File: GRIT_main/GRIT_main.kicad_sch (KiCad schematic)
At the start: 1 part, among them J1 Raspberry_Pi_4

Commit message: Updated Schematic
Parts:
- added BT1: Battery, symbol Device:Battery
- added Buck_Converter: ~, symbol Custom_Symbols:Buck_Converter_12V_to_5V
- added F1: Fuse, symbol Device:Fuse
- added M1, M2: Motor_DC, symbol Motor:Motor_DC
- added Motor_Driver_1, Motor_Driver_2, Motor_Driver_3, Motor_Driver_4: ~, symbol Custom_Symbols:12V_Motor_Controller
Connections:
- net at J1.32 (GPIO12/PWM0): now also Motor_Driver_1.3 (RPWM), Motor_Driver_1.4 (LPWM)
- net at J1.33 (GPIO13/PWM1): now also Motor_Driver_2.3 (RPWM), Motor_Driver_2.4 (LPWM)
- new net: Buck_Converter. (4), F1.1, Motor_Driver_1.2 (B+), Motor_Driver_2.2 (B+)
- new net: Buck_Converter. (4), Motor_Driver_1.1 (Vcc), Motor_Driver_2.1 (Vcc)
- new net: BT1.2 (-), Buck_Converter. (4), Motor_Driver_1.7 (B-), Motor_Driver_2.7 (B-)
- new net: Buck_Converter. (4), Motor_Driver_1.8 (GND), Motor_Driver_2.8 (GND)
- new net: M2.1 (+), Motor_Driver_2.12 (M+)
- new net: M2.2 (-), Motor_Driver_2.11 (M-)
- new net: BT1.1 (+), F1.2
- new net: M1.1 (+), Motor_Driver_1.12 (M+)
- new net: M1.2 (-), Motor_Driver_1.11 (M-)
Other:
- moved on the sheet: J1

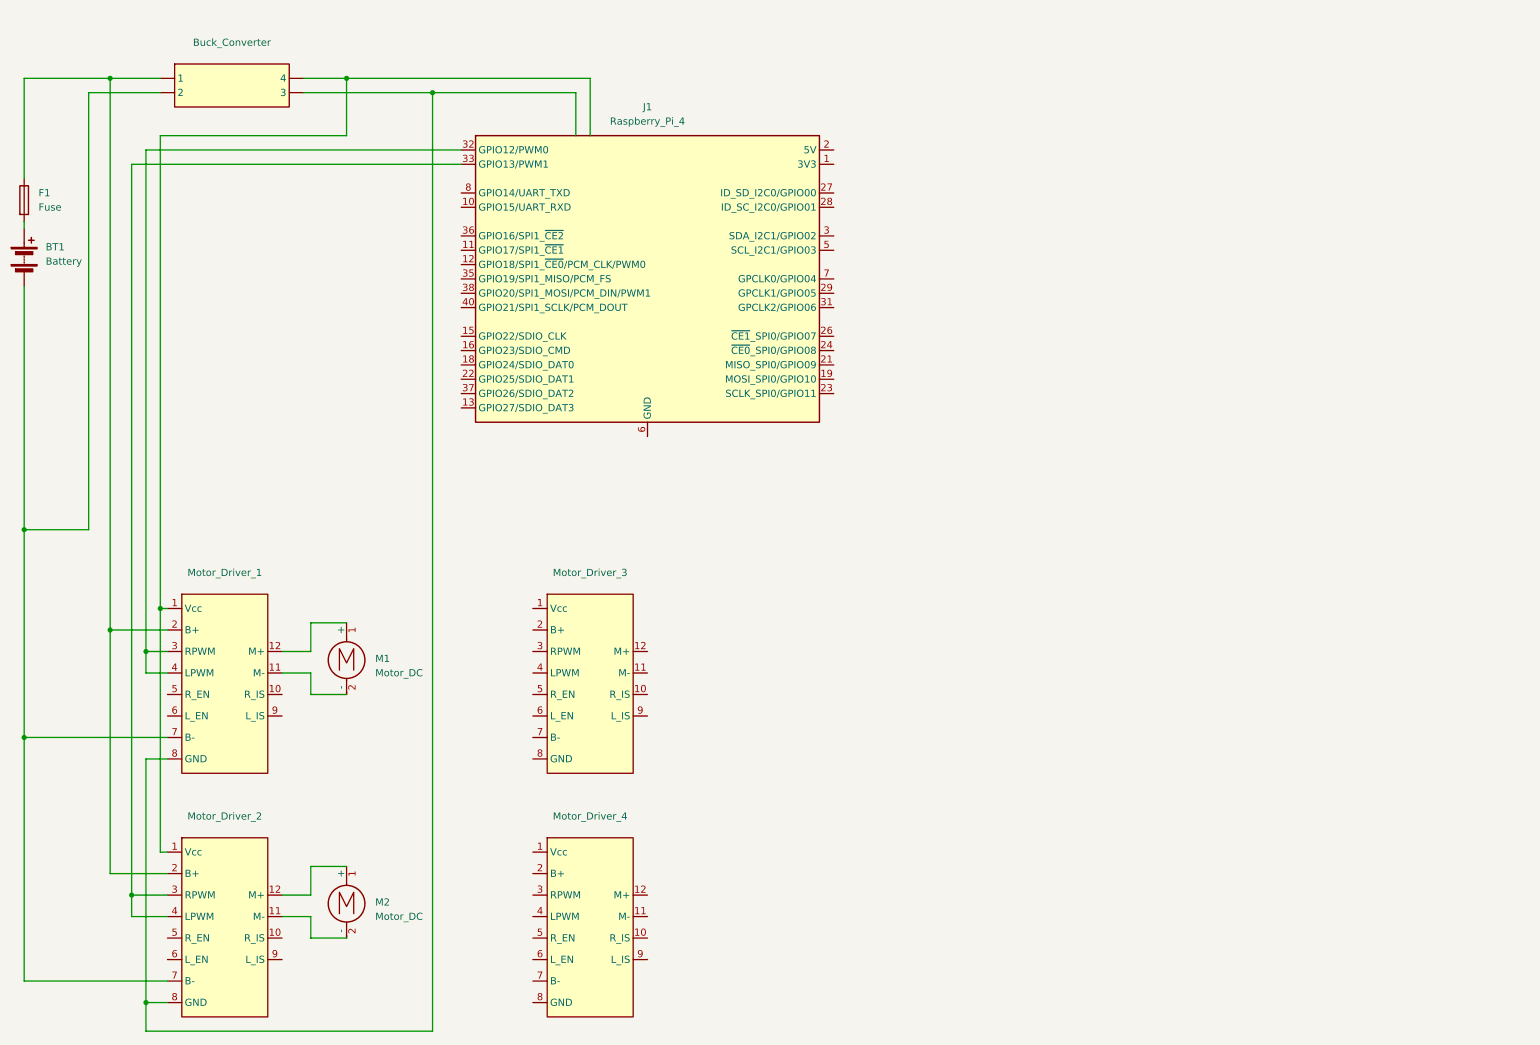
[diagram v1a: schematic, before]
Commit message: Updated Schematic
Added GPS, IMU, and Ultrasonic sensors to schematic. Also wired the other two motor drivers to the motors.
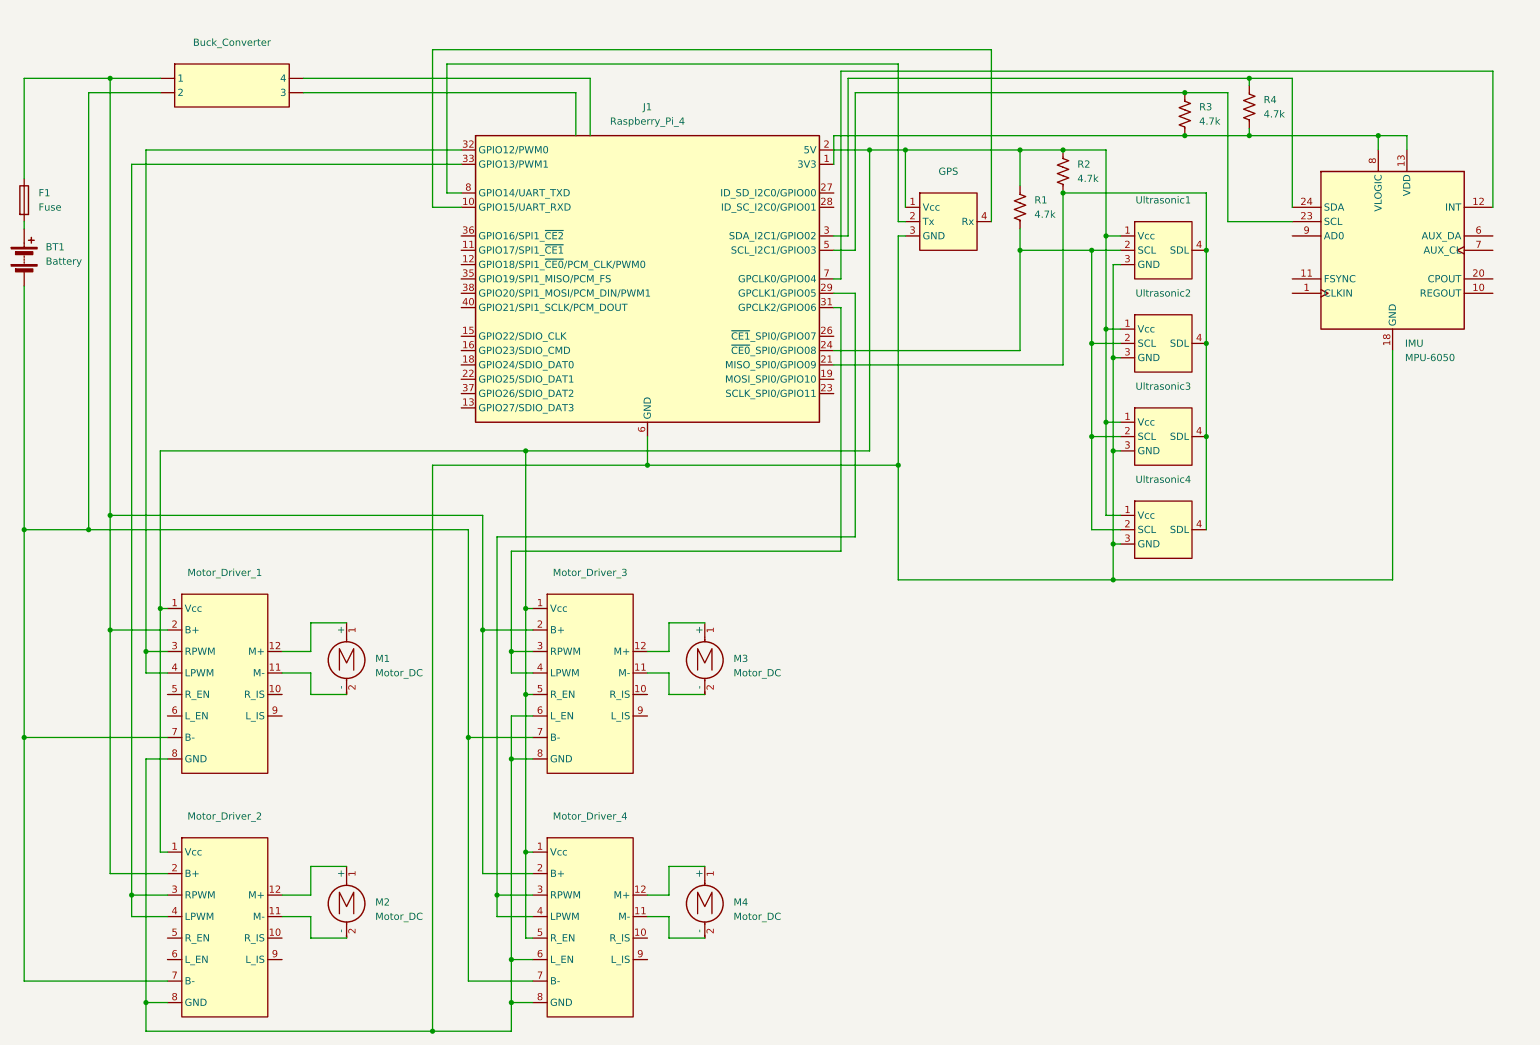
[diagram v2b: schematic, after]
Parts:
- added GPS: ~, symbol Custom_Symbols:NEO_6M_GPS
- added IMU: MPU-6050, Sensor_Motion:InvenSense_QFN-24_4x4mm_P0.5mm, symbol Sensor_Motion:MPU-6050
- added M3, M4: Motor_DC, symbol Motor:Motor_DC
- added R1, R2, R3, R4: 4.7k, symbol Device:R_US
- added Ultrasonic1, Ultrasonic2, Ultrasonic3, Ultrasonic4: ~, symbol Custom_Symbols:I2C_Ultrasonic_Sensor
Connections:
- net at Motor_Driver_3.1 (Vcc): now also J1.2 (5V), J1.4 (5V), Motor_Driver_1.1 (Vcc), Motor_Driver_2.1 (Vcc), Motor_Driver_3.5 (R_EN), Motor_Driver_4.1 (Vcc), Motor_Driver_4.5 (R_EN), GPS.1 (Vcc), R1.1, R2.1, Ultrasonic1.1 (Vcc), Ultrasonic2.1 (Vcc), Ultrasonic3.1 (Vcc), Ultrasonic4.1 (Vcc)
- net at Motor_Driver_3.11 (M-): now also M3.2 (-)
- net at Motor_Driver_3.12 (M+): now also M3.1 (+)
- net at Motor_Driver_3.2 (B+): now also Buck_Converter. (4), F1.1, Motor_Driver_1.2 (B+), Motor_Driver_2.2 (B+), Motor_Driver_4.2 (B+)
- net at Motor_Driver_3.3 (RPWM): now also J1.31 (GPCLK2/GPIO06), Motor_Driver_3.4 (LPWM)
- net at Motor_Driver_3.6 (L_EN): now also J1.14 (GND), J1.20 (GND), J1.25 (GND), J1.30 (GND), J1.34 (GND), J1.39 (GND), J1.6 (GND), J1.9 (GND), Motor_Driver_1.8 (GND), Motor_Driver_2.8 (GND), Motor_Driver_3.8 (GND), Motor_Driver_4.6 (L_EN), Motor_Driver_4.8 (GND), GPS.3 (GND), IMU.18 (GND), Ultrasonic1.3 (GND), Ultrasonic2.3 (GND), Ultrasonic3.3 (GND), Ultrasonic4.3 (GND)
- net at Motor_Driver_3.7 (B-): now also BT1.2 (-), Buck_Converter. (4), Motor_Driver_1.7 (B-), Motor_Driver_2.7 (B-), Motor_Driver_4.7 (B-)
- net at Motor_Driver_4.11 (M-): now also M4.2 (-)
- net at Motor_Driver_4.12 (M+): now also M4.1 (+)
- net at Motor_Driver_4.3 (RPWM): now also J1.29 (GPCLK1/GPIO05), Motor_Driver_4.4 (LPWM)
- net at J1.1 (3V3), J1.17 (3V3): now also IMU.13 (VDD), IMU.8 (VLOGIC), R3.2, R4.2
- net at J1.10 (GPIO15/UART_RXD): now also GPS.4 (Rx)
- net at J1.21 (MISO_SPI0/GPIO09): now also R2.2, Ultrasonic1.4 (SDL), Ultrasonic2.4 (SDL), Ultrasonic3.4 (SDL), Ultrasonic4.4 (SDL)
- net at J1.24 (~{CE0}_SPI0/GPIO08): now also R1.2, Ultrasonic1.2 (SCL), Ultrasonic2.2 (SCL), Ultrasonic3.2 (SCL), Ultrasonic4.2 (SCL)
- net at J1.3 (SDA_I2C1/GPIO02): now also IMU.24 (SDA), R4.1
- net at J1.5 (SCL_I2C1/GPIO03): now also IMU.23 (SCL), R3.1
- net at J1.7 (GPCLK0/GPIO04): now also IMU.12 (INT)
- net at J1.8 (GPIO14/UART_TXD): now also GPS.2 (Tx)
- now unconnected: Buck_Converter. (4), Buck_Converter. (4), Buck_Converter. (4), Buck_Converter. (4)

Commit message: Updated Schematic
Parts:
- added D1, D2: LED, symbol Device:LED
- added LCD: ~, symbol Custom_Symbols:I2C_LCD_Screen
- added LimitSwitch: ~, symbol Switch:SW_SPDT_XKB_DMx-xxxx-1
- added Q1: IRLZ34N, Package_TO_SOT_THT:TO-220-3_Vertical, symbol Transistor_FET:IRLZ34N
- added Ultrasonic5, Ultrasonic6, Ultrasonic7: ~, symbol Custom_Symbols:I2C_Ultrasonic_Sensor
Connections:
- net at GPS.3 (GND), IMU.18 (GND), J1.14 (GND)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: now also LCD.3 (GND), LimitSwitch.1 (A), Ultrasonic5.3 (GND), Ultrasonic6.3 (GND), Ultrasonic7.3 (GND)
- net at GPS.1 (Vcc), J1.2 (5V), J1.4 (5V)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: now also LCD.1 (Vcc), Ultrasonic5.1 (Vcc), Ultrasonic6.1 (Vcc), Ultrasonic7.1 (Vcc)
- net at Buck_Converter. (4), F1.1, Motor_Driver_1.2 (B+)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: now also Q1.2 (D)
- net at BT1.2 (-), Buck_Converter. (4), Motor_Driver_1.7 (B-)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: now also D2.1 (K)
- net at J1.13 (GPIO27/SDIO_DAT3): now also LimitSwitch.3 (C)
- net at J1.19 (MOSI_SPI0/GPIO10): now also LCD.2 (SCL)
- net at J1.21 (MISO_SPI0/GPIO09), R2.2, Ultrasonic1.4 (SDL)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: now also Ultrasonic5.4 (SDL), Ultrasonic6.4 (SDL), Ultrasonic7.4 (SDL)
- net at J1.23 (SCLK_SPI0/GPIO11): now also LCD.4 (SDA)
- net at J1.24 (~{CE0}_SPI0/GPIO08), R1.2, Ultrasonic1.2 (SCL)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: now also Ultrasonic5.2 (SCL), Ultrasonic6.2 (SCL), Ultrasonic7.2 (SCL)
- net at J1.36 (GPIO16/SPI1_~{CE2}): now also Q1.1 (G)
- new net: D1.2 (A), Q1.3 (S)
- new net: D1.1 (K), D2.2 (A)
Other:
- moved on the sheet: BT1, F1

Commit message: Updated Design
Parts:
- removed Ultrasonic1, Ultrasonic2, Ultrasonic3, Ultrasonic4, Ultrasonic5, Ultrasonic6, Ultrasonic7: ~, symbol Custom_Symbols:I2C_Ultrasonic_Sensor
- added U1: Raspberry_Pi_Pico, Package_DFN_QFN:QFN-56-1EP_7x7mm_P0.4mm_EP3.2x3.2mm, symbol MCU_RaspberryPi:RP2040
- added US1, US2, US3, US4, US5, US6, US7: ~, symbol Custom_Symbols:I2C_Ultrasonic_Sensor
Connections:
- net at GPS.1 (Vcc), J1.2 (5V), J1.4 (5V)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: no longer R1.1, R2.1
- net at R1.2: now also J1.21 (MISO_SPI0/GPIO09), U1.28 (GPIO17); no longer J1.24 (~{CE0}_SPI0/GPIO08)
- net at GPS.3 (GND), IMU.18 (GND), J1.14 (GND)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: now also U1.57 (GND), US1.3 (GND), US2.3 (GND), US3.3 (GND), US4.3 (GND), US5.3 (GND), US6.3 (GND), US7.3 (GND)
- net at R2.2: now also J1.24 (~{CE0}_SPI0/GPIO08), U1.27 (GPIO16); no longer J1.21 (MISO_SPI0/GPIO09)
- net at IMU.13 (VDD), IMU.8 (VLOGIC), J1.1 (3V3)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: now also R1.1, R2.1
- net at IMU.23 (SCL), J1.5 (SCL_I2C1/GPIO03): now also R4.1; no longer R3.1
- net at IMU.24 (SDA), J1.3 (SDA_I2C1/GPIO02): now also R3.1; no longer R4.1
- new net: U1.4 (GPIO2), US1.1 (Trig)
- new net: U1.5 (GPIO3), US1.2 (Echo)
- new net: Buck_Converter. (4), U1.48 (USB_VDD), US1.4 (Vcc), US2.4 (Vcc), US3.4 (Vcc), US4.4 (Vcc), US5.4 (Vcc), US6.4 (Vcc), US7.4 (Vcc)
- new net: U1.15 (GPIO12), US6.1 (Trig)
- new net: U1.16 (GPIO13), US6.2 (Echo)
- new net: U1.6 (GPIO4), US2.1 (Trig)
- new net: U1.7 (GPIO5), US2.2 (Echo)
- new net: U1.17 (GPIO14), US7.1 (Trig)
- new net: U1.18 (GPIO15), US7.2 (Echo)
- new net: U1.11 (GPIO8), US4.1 (Trig)
- new net: U1.12 (GPIO9), US4.2 (Echo)
- new net: U1.8 (GPIO6), US3.1 (Trig)
- new net: U1.9 (GPIO7), US3.2 (Echo)
- new net: U1.1 (IOVDD), U1.10 (IOVDD), U1.22 (IOVDD), U1.33 (IOVDD), U1.42 (IOVDD), U1.49 (IOVDD)
- new net: U1.13 (GPIO10), US5.1 (Trig)
- new net: U1.14 (GPIO11), US5.2 (Echo)
- new net: U1.23 (DVDD), U1.50 (DVDD)
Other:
- moved on the sheet: IMU, LCD, LimitSwitch

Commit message: Updated and Added PDF
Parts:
- removed R3, R4: 4.7k, symbol Device:R_US
- M1: value Motor_DC -> Drive Motor Left
- M2: value Motor_DC -> Drive Motor Right
- M3: value Motor_DC -> Rotating Drum
- M4: value Motor_DC -> Flywheel
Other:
- note added: "GRIT Total Schematic"
- note added: "Go Granular"
